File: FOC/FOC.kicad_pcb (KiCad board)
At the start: 4 copper layers, 79 x 34.9 mm, 74 parts, among them J1 encoder_conn, J2 Conn_ARM_JTAG_SWD_10, J3 UART_debug, J4 XT30PW-M, J5 Conn_01x04_Socket, J6 Conn_01x04_Socket, J7 Conn_01x03_Socket, SW1 SW_Push, SW2 SW_Push, U1 STM32G431CBTx, U2 SN65HVD230, U3 TPS54202DDC, U4 AP2112K-3.3, U5 DRV8313PWP, Y1 Crystal_GND24

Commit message: some layout art
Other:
- board text added: "Servo Controller Made by Katherine Chen <3"
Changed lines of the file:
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@@
 		(layer "Edge.Cuts")
+	)
+	(gr_text "Servo Controller \nMade by Katherine Chen <3\n"
+		(at 105.6 41.4 0)
+		(layer "B.SilkS")
+		(effects
+			(font
+				(size 0.7 0.7)
+				(thickness 0.09)
+			)
+			(justify left bottom mirror)
+		)
 	)
 	(segment

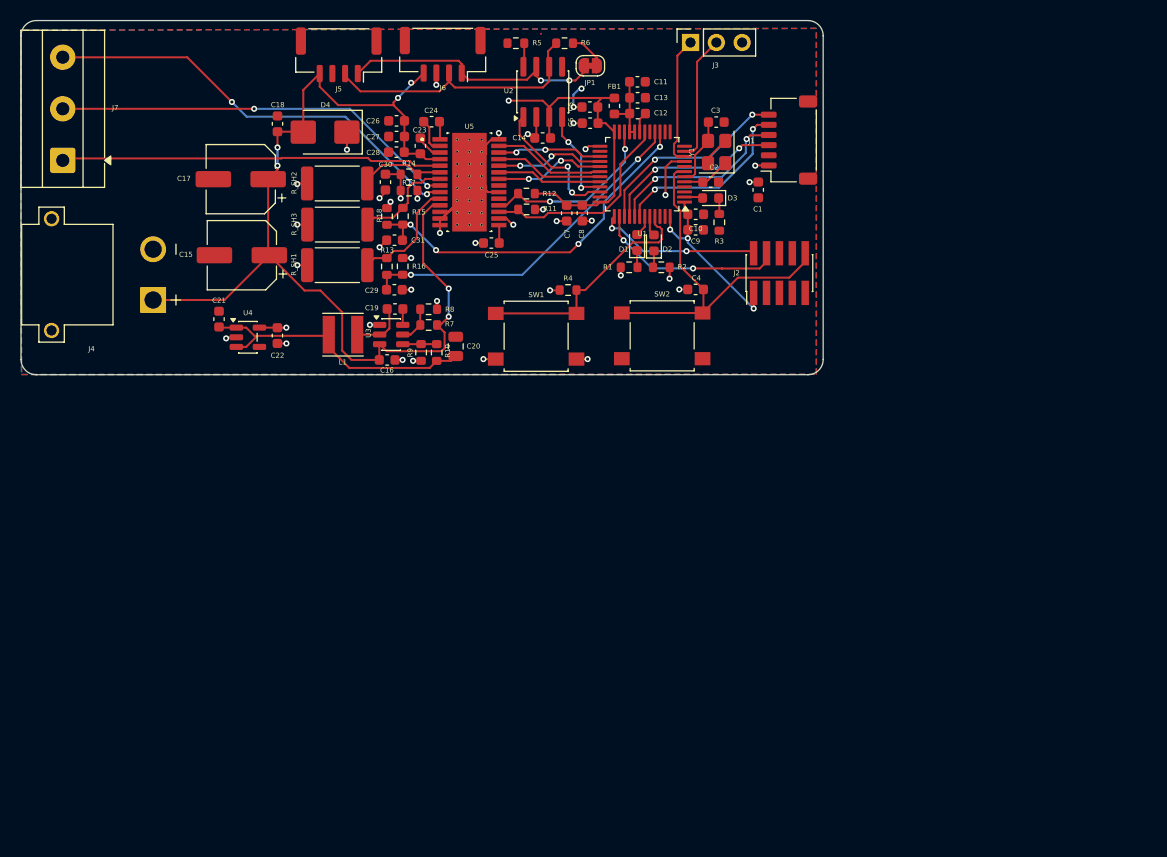
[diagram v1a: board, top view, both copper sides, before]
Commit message: EMI noise reduction; stitch time
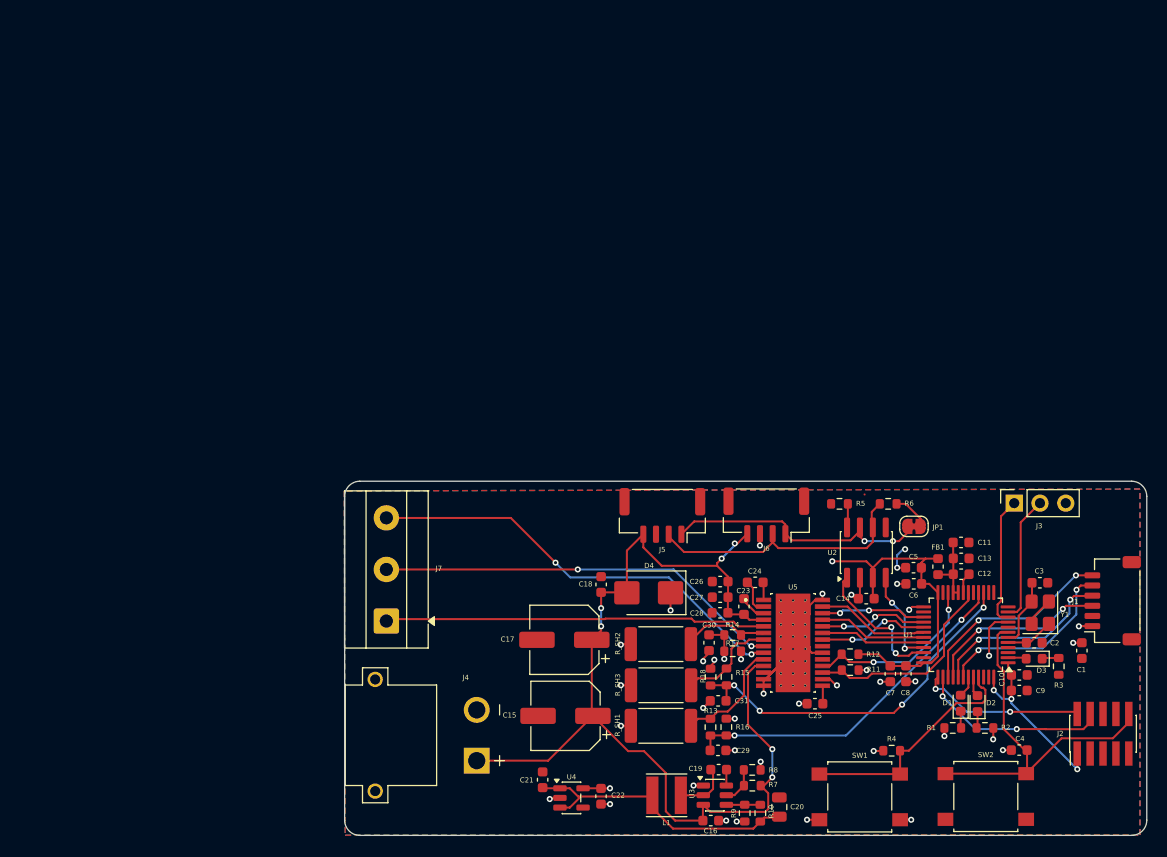
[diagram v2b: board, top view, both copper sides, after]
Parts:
- added G***: LOGO, logo:stitch, B.Cu at (126.3, 90.8)
- moved C10 55.4 mm to (178.9, 100.3)
- moved C12 55.4 mm to (173.2, 90.4)
- moved C13 55.4 mm to (173.2, 88.9)
- moved C15 55.4 mm to (134.2, 104.4)
- moved C21 55.4 mm to (132.0, 110.7)
- moved C22 55.4 mm to (137.7, 112.3)
- moved C28 55.4 mm to (149.4, 94.2)
- moved C3 55.4 mm to (180.9, 91.3)
- moved C8 55.4 mm to (167.8, 100.2)
- moved C9 55.4 mm to (178.9, 101.9)
- moved D3 55.4 mm to (180.4, 98.7)
- moved FB1 55.4 mm to (170.9, 89.7)
- moved J2 55.4 mm to (187.2, 106.1)
- moved J3 55.4 mm to (178.4, 83.4)
- moved J6 55.4 mm to (154.0, 84.6)
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
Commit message: mech considered; mounting holes; teardrops
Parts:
- added H1: MountingHole_Pad, MountingHole:MountingHole_2.1mm, F.Cu at (189.1, 83.7)
- added H2: MountingHole_Pad, MountingHole:MountingHole_2.1mm, F.Cu at (189.1, 113.8)
- added H3: MountingHole_Pad, MountingHole:MountingHole_2.1mm, F.Cu at (129.4, 113.8)
- added H4: MountingHole_Pad, MountingHole:MountingHole_2.1mm, F.Cu at (129.4, 83.6)
- moved G*** 1.00 mm to (126.4, 91.8)

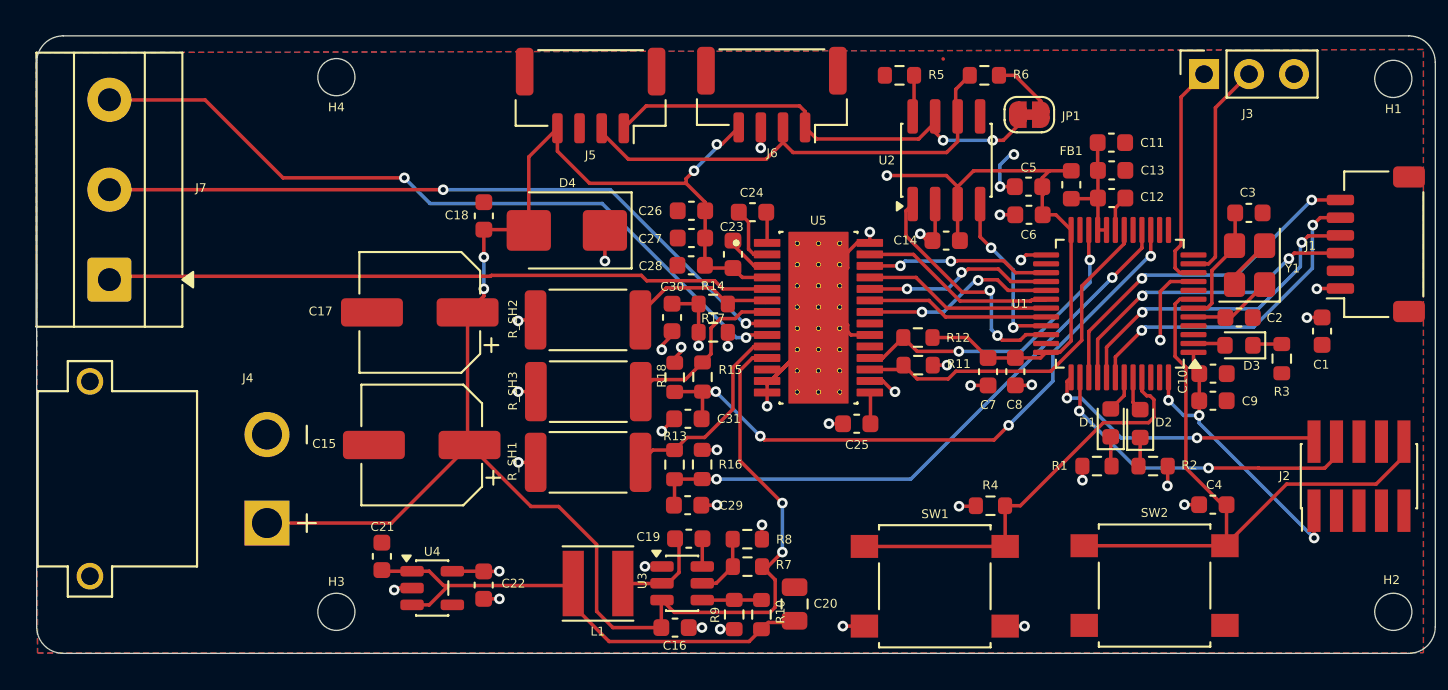
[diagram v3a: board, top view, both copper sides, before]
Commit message: traces cleanup
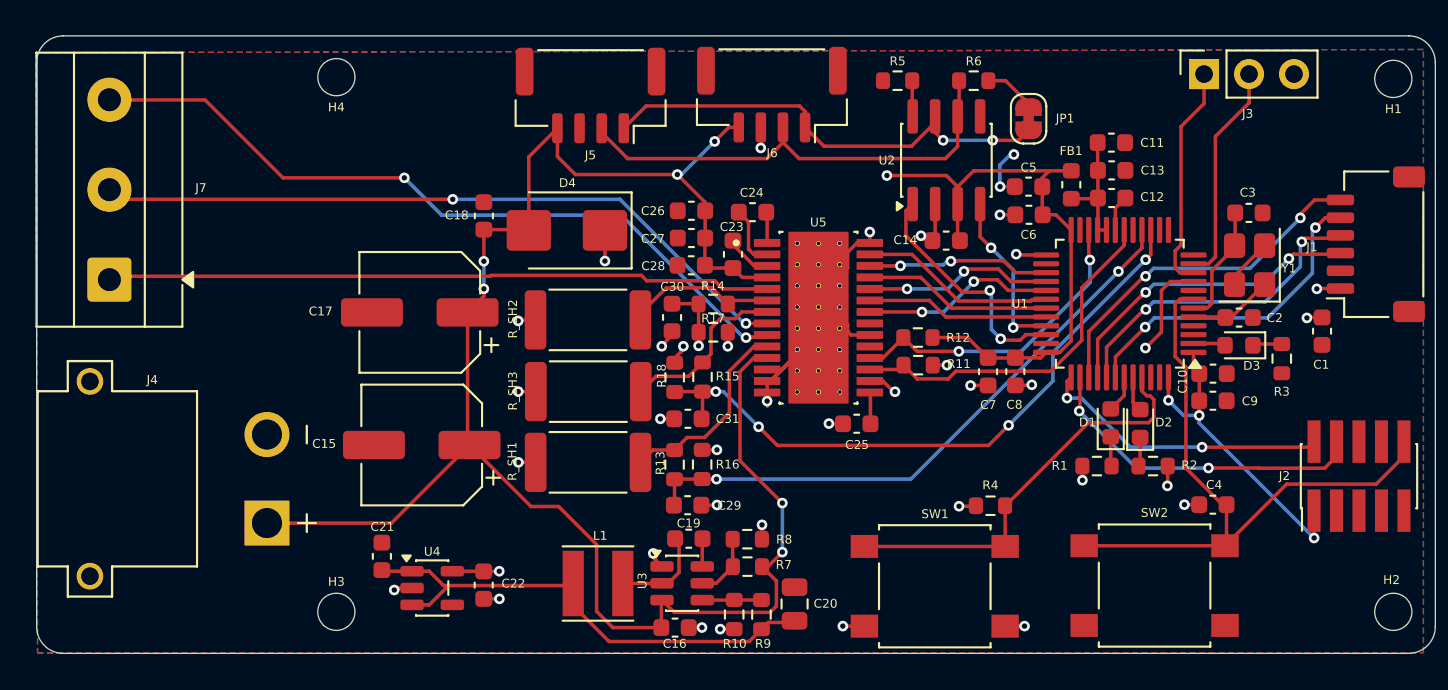
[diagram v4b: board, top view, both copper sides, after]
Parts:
- moved G*** 2.06 mm to (128.4, 92.3)
- moved R6 0.67 mm to (165.4, 83.8)
- moved R5 0.32 mm to (161.1, 83.8)
- moved JP1 0.24 mm to (168.5, 86.0), turned to -90 degrees
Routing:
- net +3.3V: track 75.8 -> 77.4 mm
- net GND: track 58.4 -> 57.3 mm
- net Net-(JP1-A): track 3.73 -> 3.01 mm

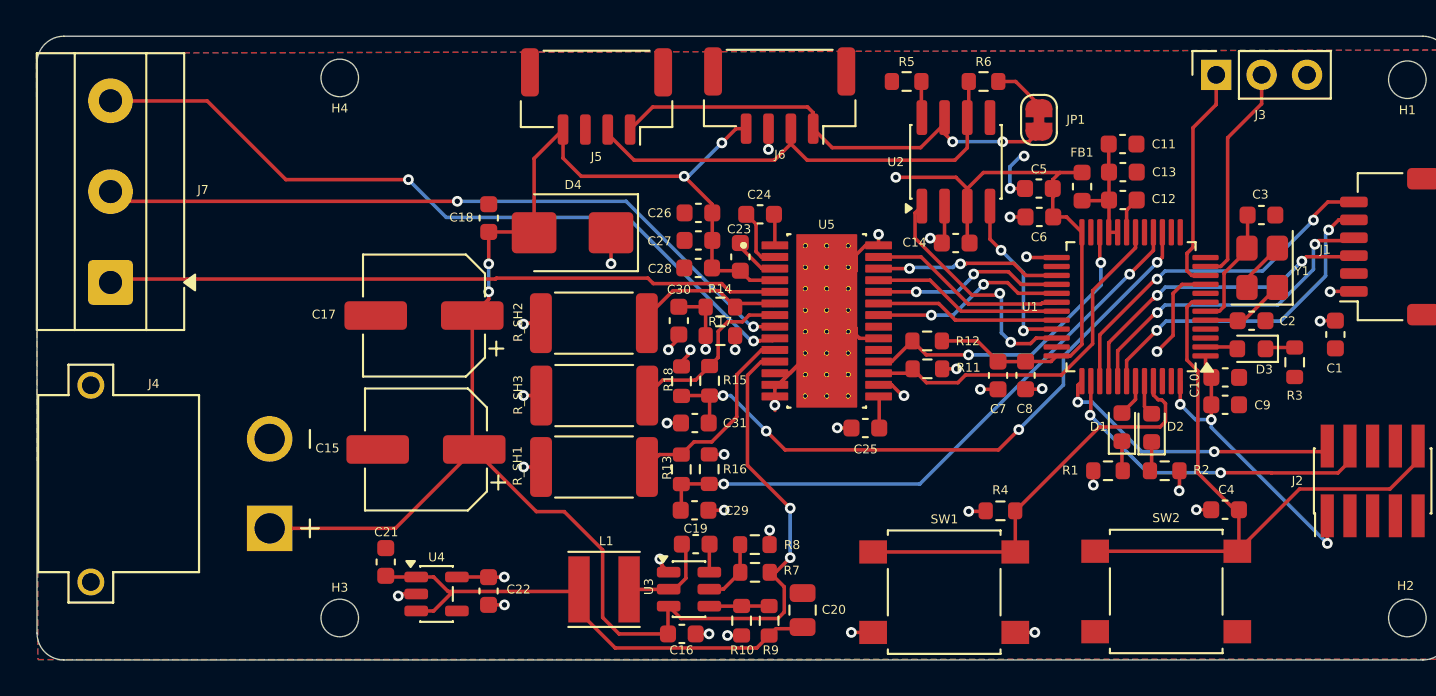
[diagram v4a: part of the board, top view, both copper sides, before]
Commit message: return path improved; debug power traces
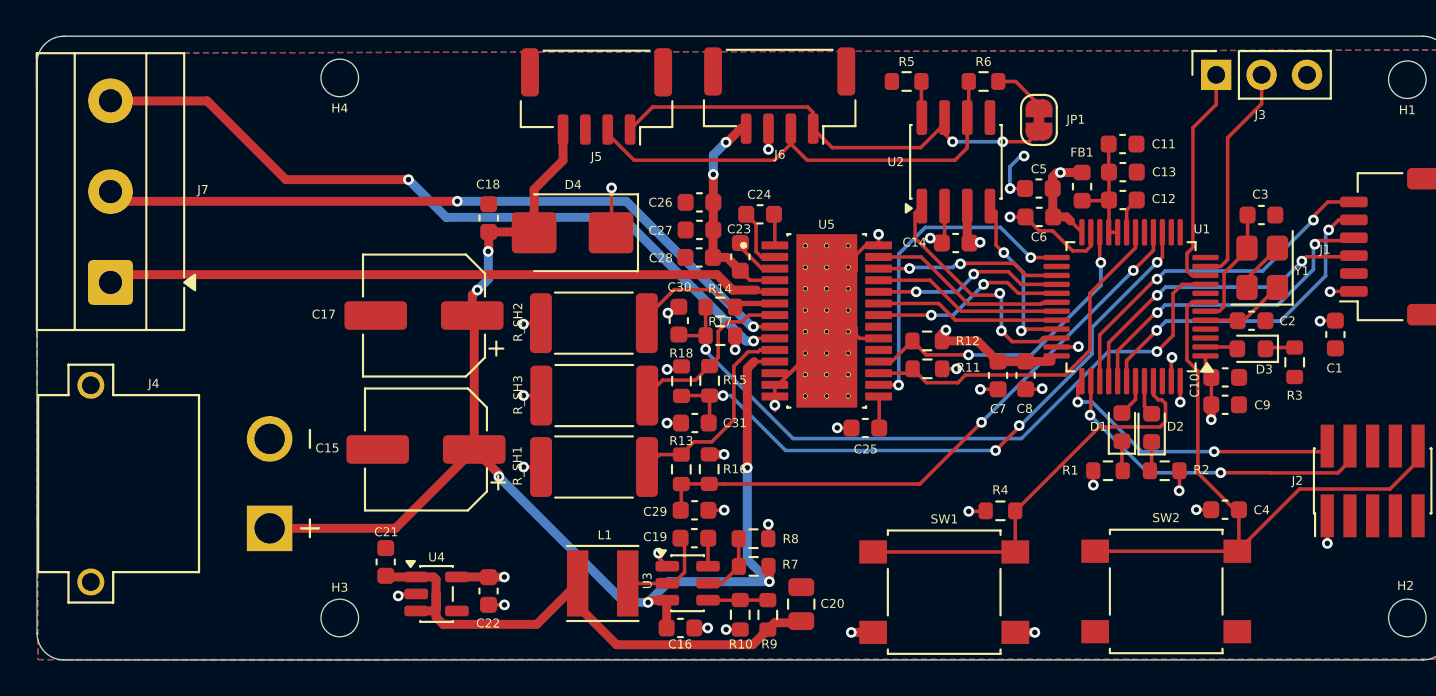
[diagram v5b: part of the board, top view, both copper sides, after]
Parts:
- moved C27 0.59 mm to (149.5, 92.1)
- moved C26 0.59 mm to (149.5, 90.6)
- moved C28 0.59 mm to (149.5, 93.6)
- moved C19 0.34 mm to (149.2, 109.3)
- moved L1 0.34 mm to (144.1, 111.9)
- moved R10 0.34 mm to (151.8, 113.6)
- moved R7 0.34 mm to (152.5, 110.9)
- moved R8 0.34 mm to (152.5, 109.4)
- moved R9 0.34 mm to (153.3, 113.6)
- moved U3 0.34 mm to (148.9, 111.9)
- moved C16 0.34 mm to (148.5, 114.4)
- moved C20 0.34 mm to (155.2, 113.0)
- turned C30 to 90 degrees
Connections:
- U1 pad 23: unconnected-(U1-VSS-Pad23)_1 -> GND
- U1 pad 35: unconnected-(U1-VSS-Pad23) -> GND
- U1 pad 47: unconnected-(U1-VSS-Pad23)_2 -> GND
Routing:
- net +3.3V: track 77.4 -> 32.5 mm, vias 12 -> 14
- net VM: track 100.7 -> 85.4 mm, vias 6 -> 8
- net GND: track 57.3 -> 65.8 mm, vias 28 -> 30
- net DRV_RST: track 14.3 -> 18.6 mm
- net ISNS_A: track 36.5 -> 39.1 mm
- net +5V: track 28.8 -> 31.2 mm
